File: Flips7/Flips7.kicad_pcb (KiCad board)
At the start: 2 copper layers, 100 x 100 mm, 21 parts, among them CN1 Conn_02x17_Odd_Even, CN2 Conn_02x17_Odd_Even, U1 FP2800A, U2 FP2800A, U3 FP2800A

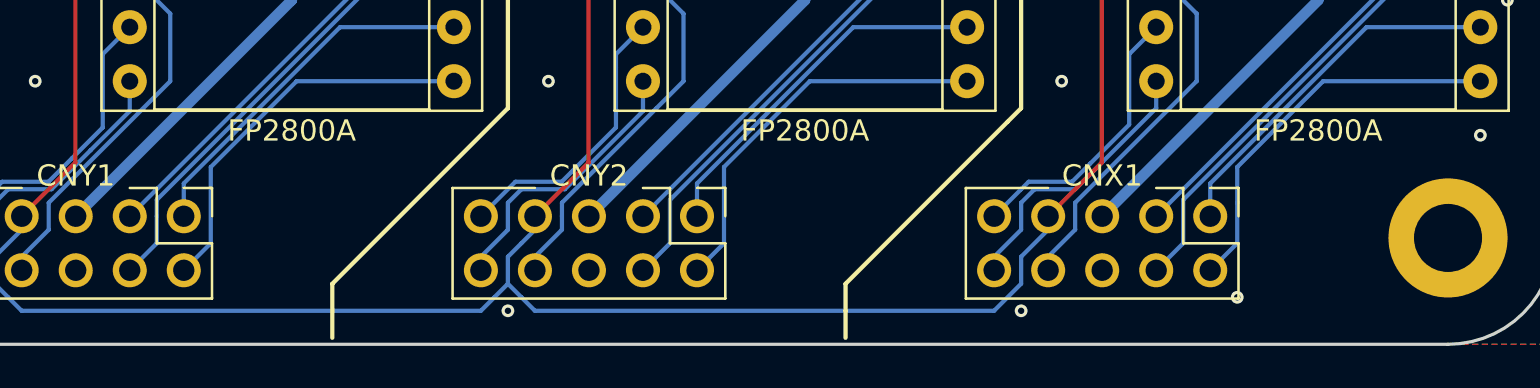
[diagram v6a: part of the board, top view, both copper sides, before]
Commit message: adding pull downs for ENABLE pins
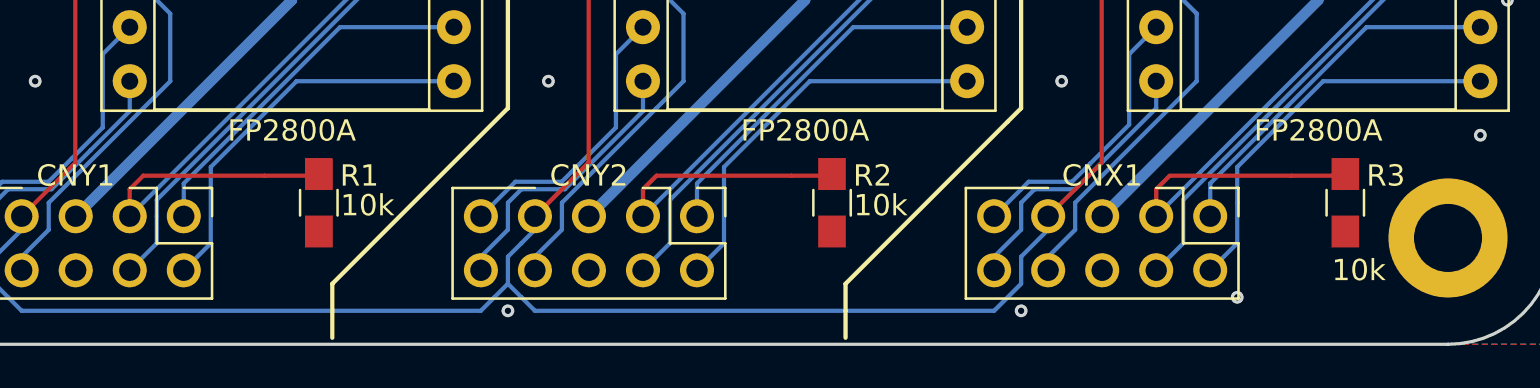
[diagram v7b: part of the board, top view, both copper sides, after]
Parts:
- added R1: 10k, Resistors_SMD:R_0805_HandSoldering, F.Cu at (67.3, 118.7)
- added R2: 10k, Resistors_SMD:R_0805_HandSoldering, F.Cu at (91.4, 118.7)
- added R3: 10k, Resistors_SMD:R_0805_HandSoldering, F.Cu at (115.6, 118.7)
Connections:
- net /GND renamed GND
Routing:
- net /R.EN: track 21.0 -> 31.5 mm
- net /L.EN: track 21.0 -> 31.5 mm
- net /X.EN: track 21.0 -> 31.5 mm

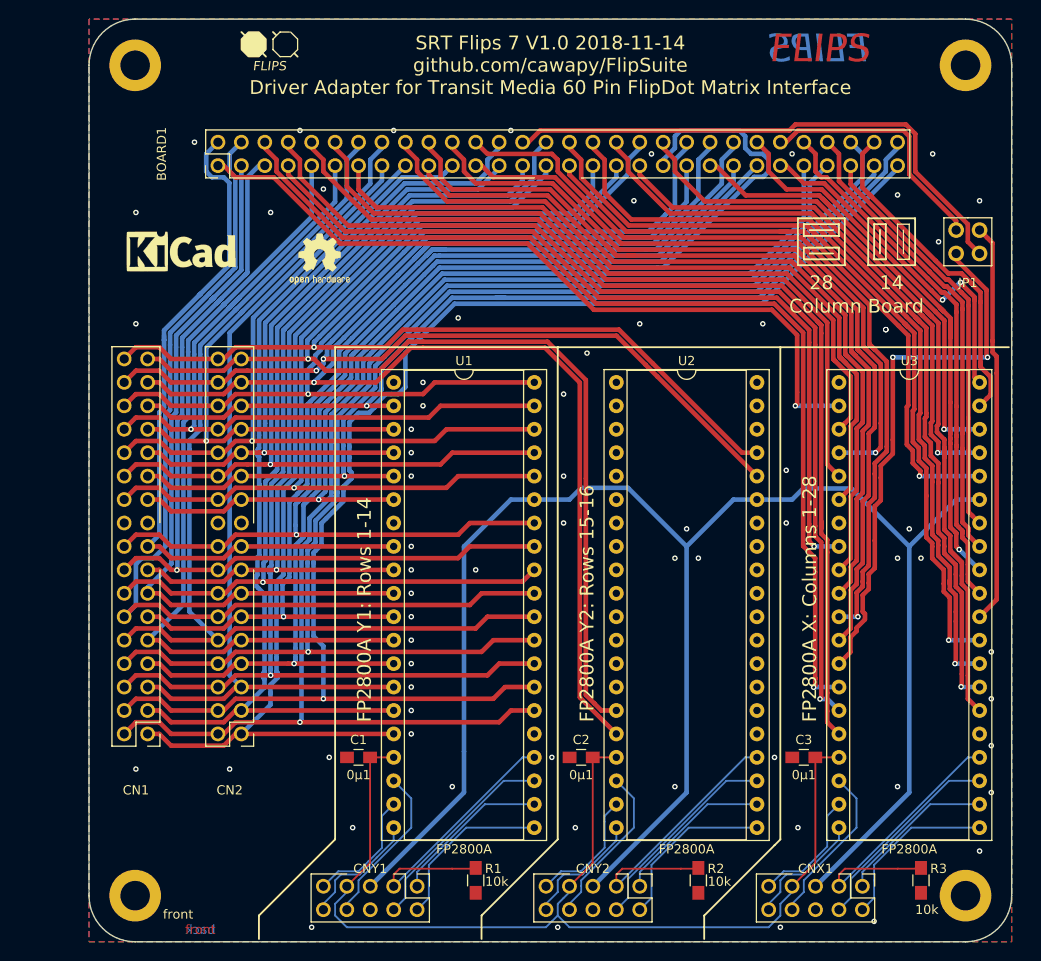
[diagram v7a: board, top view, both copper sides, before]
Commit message: rename some symbols
rename L.## and R.## nets to Y1.## and Y2.##
rename CN1 and CN2 to SHR1 and SHR2
rename U1/2/3 to IC1/2/3
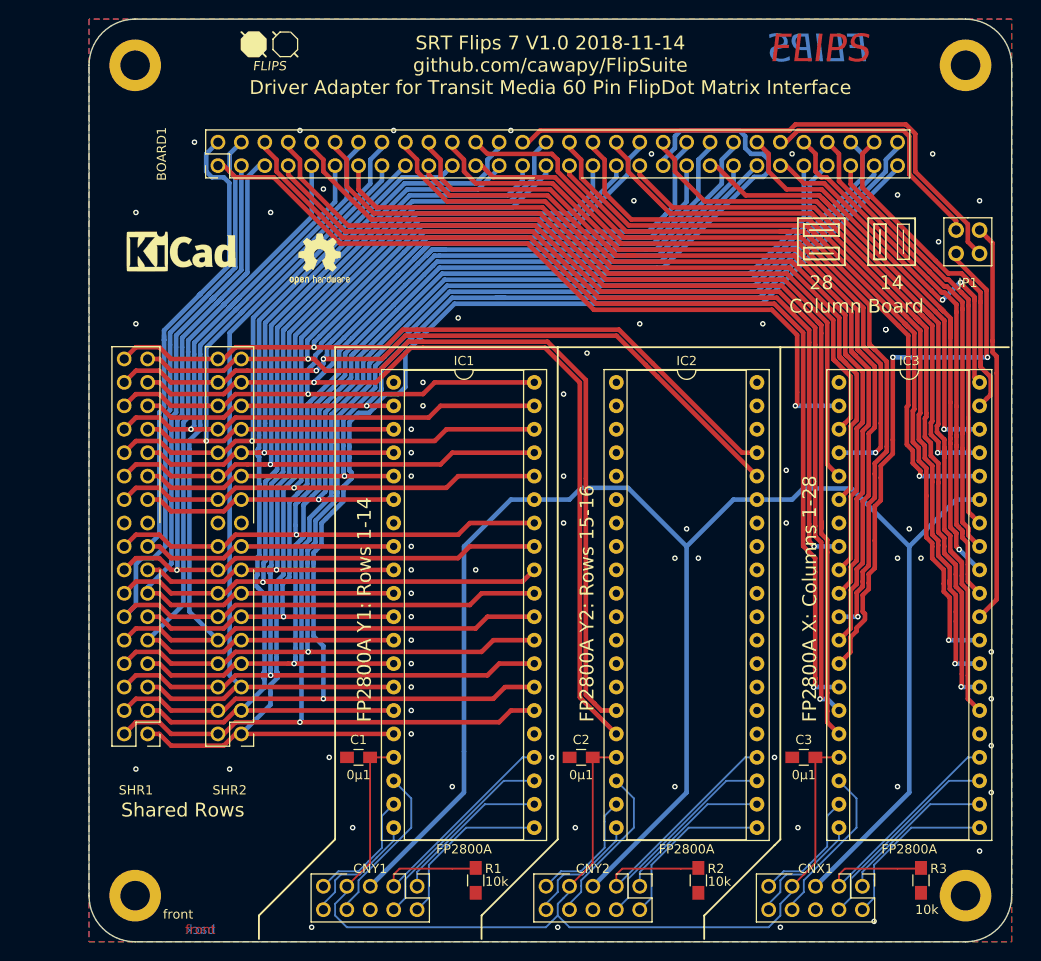
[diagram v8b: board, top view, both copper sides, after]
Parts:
- renumbered U1 to IC1, U2 to IC2, U3 to IC3, CN1 to SHR1, CN2 to SHR2
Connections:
- net /L.A0 renamed /Y1.A0
- net /L.A1 renamed /Y1.A1
- net /L.A2 renamed /Y1.A2
- net /L.B0 renamed /Y1.B0
- net /L.B1 renamed /Y1.B1
- net /L.EN renamed /Y1.EN
- net /L.POL renamed /Y1.POL
- net /R.A0 renamed /Y2.A0
- net /R.A1 renamed /Y2.A1
- net /R.A2 renamed /Y2.A2
- net /R.B0 renamed /Y2.B0
- net /R.B1 renamed /Y2.B1
- net /R.EN renamed /Y2.EN
- net /R.POL renamed /Y2.POL
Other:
- board text added: "Shared Rows"
